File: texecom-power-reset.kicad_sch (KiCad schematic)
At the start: 0 parts

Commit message: Switch to on-board relays and add wired schematic
- Replace the off-board REL-2CHAN-335V relay module with two on-board
  SRD-05VDC-SL-C relays, 2N2222A drivers, 1N4007 flyback diodes and red
  indicator LEDs; remove J5-J7, the control lead and the Q/nQ links
- Redraw the schematic with wires (power symbols only for GND/+5V),
  ERC clean and netlist verified net by net
- Use a 74HCT4538 at 5V for the hardware timeout, with 1k GPIO series
  resistors and 100R CEXT power-down protection
- Update README (requirements, design, bench tests, decisions) and BOM
  (Micro Robotics / Communica sourcing with stock status)
- Keep earlier schematic versions in backup/ for reference
- Add .gitignore and .gitattributes (LF line endings for KiCad files)

Co-Authored-By: Claude Opus 5.5 <noreply@anthropic.com>
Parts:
- added C1: 100uF, Capacitor_THT:CP_Radial_D6.3mm_P2.50mm, symbol Device:C_Polarized
- added C2, C4, C7, C8: 100nF, Capacitor_THT:C_Disc_D5.0mm_W2.5mm_P5.00mm, symbol Device:C
- added C3: 10uF, Capacitor_THT:CP_Radial_D4.0mm_P1.50mm, symbol Device:C_Polarized
- added C5, C6: 10uF, Capacitor_SMD:C_1206_3216Metric_Pad1.33x1.80mm_HandSolder, symbol Device:C
- added D1, D3: 1N5822, Diode_THT:D_DO-201AD_P15.24mm_Horizontal, symbol Diode:1N5822
- added D2: P6KE18A, Diode_THT:D_DO-15_P10.16mm_Horizontal, symbol Device:D_Zener
- added D4, D5: 1N4007, Diode_THT:D_DO-41_SOD81_P10.16mm_Horizontal, symbol Device:D
- added D6, D7: RED, LED_THT:LED_D3.0mm, symbol Device:LED
- added F1: PTC 0.5A, Fuse:Fuse_1206_3216Metric_Pad1.42x1.75mm_HandSolder, symbol Device:Polyfuse
- added J1: BAT IN, TerminalBlock_Phoenix:TerminalBlock_Phoenix_MKDS-1,5-2_1x02_P5.00mm_Horizontal, symbol Connector:Screw_Terminal_01x02
- added J2: BAT OUT, TerminalBlock_Phoenix:TerminalBlock_Phoenix_MKDS-1,5-2_1x02_P5.00mm_Horizontal, symbol Connector:Screw_Terminal_01x02
- added J3: AC IN, TerminalBlock_Phoenix:TerminalBlock_Phoenix_MKDS-1,5-2_1x02_P5.00mm_Horizontal, symbol Connector:Screw_Terminal_01x02
- added J4: AC OUT, TerminalBlock_Phoenix:TerminalBlock_Phoenix_MKDS-1,5-2_1x02_P5.00mm_Horizontal, symbol Connector:Screw_Terminal_01x02
- added K1, K2: SRD-05VDC, Relay_THT:Relay_SPDT_SANYOU_SRD_Series_Form_C, symbol Relay:SANYOU_SRD_Form_C
- added MH1, MH2: M3, MountingHole:MountingHole_3.2mm_M3, symbol Mechanical:MountingHole
- added Q1, Q2: 2N2222A, Package_TO_SOT_THT:TO-92_Inline, symbol Transistor_BJT:PN2222A
- added R1, R2: 100k, Resistor_THT:R_Axial_DIN0207_L6.3mm_D2.5mm_P10.16mm_Horizontal, symbol Device:R
- added R10, R15, R16, R7, R8, R9: 1k, Resistor_SMD:R_1206_3216Metric_Pad1.30x1.75mm_HandSolder, symbol Device:R
- added R11, R12: 100, Resistor_SMD:R_1206_3216Metric_Pad1.30x1.75mm_HandSolder, symbol Device:R
- added R13, R14, R5, R6: 10k, Resistor_THT:R_Axial_DIN0207_L6.3mm_D2.5mm_P10.16mm_Horizontal, symbol Device:R
- added R3, R4: 1M, Resistor_THT:R_Axial_DIN0207_L6.3mm_D2.5mm_P10.16mm_Horizontal, symbol Device:R
- added U1: Pololu S9V11E2F5, texecom-power-reset:Pololu_S9V11E2x, symbol texecom-power-reset:Pololu_S9V11E2F5
- added U2: 74HCT4538, Package_DIP:DIP-16_W7.62mm_Socket, symbol 4xxx:4538
- added U3: ESP32-C3 SuperMini, texecom-power-reset:ESP32-C3-SuperMini, symbol texecom-power-reset:ESP32-C3-SuperMini
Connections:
- new net: F1.1, J1.1 (Pin_1), K1.1
- new net: D1.2 (A), F1.2
- new net: J3.1 (Pin_1), K2.1
- new net: D5.2 (A), D7.1 (K), K2.2, Q2.3 (C)
- new net: J4.1 (Pin_1), K2.4
- new net: C1.1, C2.1, D1.1 (K), D2.1 (K), U1.3 (VIN)
- new net: C8.1, R6.2, U2.12 (Clk+)
- new net: Q2.2 (B), R14.1, R8.2
- new net: C6.1, R4.2, U2.14 (RxCx)
- new net: C5.1, R3.2, U2.2 (RxCx)
- new net: R1.1, R5.1, R9.2, U2.3 (R)
- new net: C7.1, R5.2, U2.4 (Clk+)
- new net: R7.1, U2.6 (Q)
- new net: R10.1, U3.4 (IO4)
- new net: R9.1, U3.5 (IO3)
- new net: Q1.2 (B), R13.1, R7.2
- new net: D4.2 (A), D6.1 (K), K1.2, Q1.3 (C)
- new net: J3.2 (Pin_2), J4.2 (Pin_2)
- new net: R8.1, U2.10 (Q)
- new net: R10.2, R2.1, R6.1, U2.13 (R)
- new net: C6.2, R12.1
- new net: C5.2, R11.1
- new net: D7.2 (A), R16.2
- new net: D6.2 (A), R15.2
- new net: J2.1 (Pin_1), K1.4
- new net +5V: C3.1, C4.1, D3.2 (A), D4.1 (K), D5.1 (K), K1.5, K2.5, R15.1, R16.1, R3.1, R4.1, U1.1 (VOUT), U2.11 (Clk-), U2.16 (VDD), U2.5 (Clk-)
- new net +5V_MCU: D3.1 (K), U3.1 (5V)
- new net GND: C1.2, C2.2, C3.2, C4.2, C7.2, C8.2, D2.2 (A), J1.2 (Pin_2), J2.2 (Pin_2), Q1.1 (E), Q2.1 (E), R1.2, R11.2, R12.2, R13.2, R14.2, R2.2, U1.2 (GND), U2.1 (Cx), U2.15 (Cx), U2.8 (VSS), U3.2 (GND)
- no-connect marks 0 -> 17
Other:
- note added: "BAT_IN+ to relay K1 COM"
- note added: "CH1: battery relay K1 (GPIO3)"
- note added: "CH2: AC relay K2 (GPIO4)"
- note added: "CONTROLLER ESP32-C3 SuperMini (socketed)"
- note added: "HARDWARE TIMEOUT (74HCT4538 @ 5V) Relay ON = GPIO high AND < T since rising edge T = 0.7 x Rext x Cext = 0.7 x 1M x 10uF = ~7 s (Tasmota PulseTime 3.0 / 3.5 s is always shorter) R9/R10 1k: protect ESP GPIO if 5V rail is off (USB only) R11/R12 100R: TI rapid power-down protection for Cext RELAY DRIVERS Q -> R7/R8 1k -> 2N2222A (R13/R14 10k base pull-down) D4/D5 1N4007 flyback across each coil R15/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"
- note added: "PANEL AC (16VAC) J3 in -> K2 NC -> J4 out"
- note added: "PANEL BATTERY J1 in -> K1 NC -> J2 out"
- note added: "POWER: J1 battery tap (never switched) -> F1 PTC -> D1 reverse-polarity -> U1 Pololu 5V. D3 blocks USB backfeed from the SuperMini onto the +5V rail"
- note added: "U2C = power pins of U2 (same 74HCT4538 chip as U2A/U2B) Pin 16 VDD = +5V, pin 8 VSS = GND C4 100nF decoupling: place right beside pins 16 and 8 on the PCB"

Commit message: Add PCB rev A, milling footprints, fab files and project summary
- PCB rev A (92 x 70 mm, 2-layer, CNC-milled): placed and routed with the
  KiCad routing tools at 0.8 mm clearance, 15 wire-link vias, GND pours;
  DRC 0 violations / 0 unconnected, connectivity verified against schematic
- Milling footprint variants (oval enlarged pads; per-pad top keepouts on
  parts whose body covers the top pads) and custom .kicad_dru rules
- Schematic footprints assigned to the milling variants
- Gerbers (F.Cu, B.Cu, Edge.Cuts) and Excellon drill in fab/
- Copper renders and assembly drawing in docs/
- project-summary.html: one-page visual summary, linked from the README
- README: PCB section, drill table, assembly notes, decisions

Co-Authored-By: Claude Opus 5.5 <noreply@anthropic.com>
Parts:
- C1: footprint Capacitor_THT:CP_Radial_D6.3mm_P2.50mm -> texecom-power-reset:CP_Radial_D6.3mm_P2.50mm_Mill
- C2, C4, C7, C8: footprint Capacitor_THT:C_Disc_D5.0mm_W2.5mm_P5.00mm -> texecom-power-reset:C_Disc_D5.0mm_W2.5mm_P5.00mm_Mill
- C3: footprint Capacitor_THT:CP_Radial_D4.0mm_P1.50mm -> texecom-power-reset:CP_Radial_D5.0mm_P2.50mm_Mill
- D1, D3: footprint Diode_THT:D_DO-201AD_P15.24mm_Horizontal -> texecom-power-reset:D_DO-201AD_P15.24mm_Mill
- D2: footprint Diode_THT:D_DO-15_P10.16mm_Horizontal -> texecom-power-reset:D_DO-15_P10.16mm_Mill
- D4, D5: footprint Diode_THT:D_DO-41_SOD81_P10.16mm_Horizontal -> texecom-power-reset:D_DO-41_P10.16mm_Mill
- D6, D7: footprint LED_THT:LED_D3.0mm -> texecom-power-reset:LED_D3.0mm_Mill
- J1, J2, J3, J4: footprint TerminalBlock_Phoenix:TerminalBlock_Phoenix_MKDS-1,5-2_1x02_P5.00mm_Horizontal -> texecom-power-reset:KF301-2P_P5.00mm_Mill
- K1, K2: footprint Relay_THT:Relay_SPDT_SANYOU_SRD_Series_Form_C -> texecom-power-reset:Relay_SRD_Form_C_Mill
- Q1, Q2: footprint Package_TO_SOT_THT:TO-92_Inline -> texecom-power-reset:TO-92_Inline_Wide_Mill
- R1, R13, R14, R2, R3, R4, R5, R6: footprint Resistor_THT:R_Axial_DIN0207_L6.3mm_D2.5mm_P10.16mm_Horizontal -> texecom-power-reset:R_Axial_DIN0207_P10.16mm_Mill
- U1: footprint texecom-power-reset:Pololu_S9V11E2x -> texecom-power-reset:Pololu_S9V11E2x_Mill
- U2: footprint Package_DIP:DIP-16_W7.62mm_Socket -> texecom-power-reset:DIP-16_W7.62mm_Socket_Mill
- U3: footprint texecom-power-reset:ESP32-C3-SuperMini -> texecom-power-reset:ESP32-C3-SuperMini_Mill
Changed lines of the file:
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@@
 				)
     )
-    (property "Footprint" "TerminalBlock_Phoenix:TerminalBlock_Phoenix_MKDS-1,5-2_1x02_P5.00mm_Horizontal"
+    (property "Footprint" "texecom-power-reset:KF301-2P_P5.00mm_Mill"
       (at 20.32 50.8 0)
       (hide yes)
@@
 				)
     )
-    (property "Footprint" "Diode_THT:D_DO-201AD_P15.24mm_Horizontal"
+    (property "Footprint" "texecom-power-reset:D_DO-201AD_P15.24mm_Mill"
       (at 63.5 55.245 0)
       (hide yes)
@@
 					) (justify left))
     )
-    (property "Footprint" "Capacitor_THT:CP_Radial_D6.3mm_P2.50mm"
+    (property "Footprint" "texecom-power-reset:CP_Radial_D6.3mm_P2.50mm_Mill"
       (at 77.165 50.8 0)
       (hide yes)
@@
 					) (justify left))
     )
-    (property "Footprint" "Capacitor_THT:C_Disc_D5.0mm_W2.5mm_P5.00mm"
+    (property "Footprint" "texecom-power-reset:C_Disc_D5.0mm_W2.5mm_P5.00mm_Mill"
       (at 87.325 50.8 0)
       (hide yes)
@@
 					) (justify left))
     )
-    (property "Footprint" "Diode_THT:D_DO-15_P10.16mm_Horizontal"
+    (property "Footprint" "texecom-power-reset:D_DO-15_P10.16mm_Mill"
       (at 96.52 54.61 0)
       (hide yes)
@@
 				)
     )
-    (property "Footprint" "texecom-power-reset:Pololu_S9V11E2x"
+    (property "Footprint" "texecom-power-reset:Pololu_S9V11E2x_Mill"
       (at 121.92 48.26 0)
       (hide yes)
@@
 					) (justify left))
     )
-    (property "Footprint" "Capacitor_THT:CP_Radial_D4.0mm_P1.50mm"
+    (property "Footprint" "texecom-power-reset:CP_Radial_D5.0mm_P2.50mm_Mill"
       (at 140.665 50.8 0)
       (hide yes)
@@
 				)
     )
-    (property "Footprint" "Diode_THT:D_DO-201AD_P15.24mm_Horizontal"
+    (property "Footprint" "texecom-power-reset:D_DO-201AD_P15.24mm_Mill"
       (at 160.02 55.245 0)
       (hide yes)
@@
 				)
     )
-    (property "Footprint" "texecom-power-reset:ESP32-C3-SuperMini"
+    (property "Footprint" "texecom-power-reset:ESP32-C3-SuperMini_Mill"
       (at 48.26 190.5 0)
       (hide yes)
@@
 					) (justify left))
     )
-    (property "Footprint" "TerminalBlock_Phoenix:TerminalBlock_Phoenix_MKDS-1,5-2_1x02_P5.00mm_Horizontal"
+    (property "Footprint" "texecom-power-reset:KF301-2P_P5.00mm_Mill"
       (at 254 177.8 0)
       (hide yes)
@@
 					) (justify left))
     )
-    (property "Footprint" "TerminalBlock_Phoenix:TerminalBlock_Phoenix_MKDS-1,5-2_1x02_P5.00mm_Horizontal"
+    (property "Footprint" "texecom-power-reset:KF301-2P_P5.00mm_Mill"
       (at 254 91.44 0)
       (hide yes)
@@
 					) (justify left))
     )
-    (property "Footprint" "TerminalBlock_Phoenix:TerminalBlock_Phoenix_MKDS-1,5-2_1x02_P5.00mm_Horizontal"
+    (property "Footprint" "texecom-power-reset:KF301-2P_P5.00mm_Mill"
       (at 254 71.12 0)
       (hide yes)
@@
 					) (justify left))
     )
-    (property "Footprint" "Capacitor_THT:C_Disc_D5.0mm_W2.5mm_P5.00mm"
+    (property "Footprint" "texecom-power-reset:C_Disc_D5.0mm_W2.5mm_P5.00mm_Mill"
       (at 336.245 120.65 0)
       (hide yes)
@@
 					) (justify left))
     )
-    (property "Footprint" "Resistor_THT:R_Axial_DIN0207_L6.3mm_D2.5mm_P10.16mm_Horizontal"
+    (property "Footprint" "texecom-power-reset:R_Axial_DIN0207_P10.16mm_Mill"
       (at 97.282 118.11 90)
       (hide yes)
@@
 				)
     )
-    (property "Footprint" "Resistor_THT:R_Axial_DIN0207_L6.3mm_D2.5mm_P10.16mm_Horizontal"
+    (property "Footprint" "texecom-power-reset:R_Axial_DIN0207_P10.16mm_Mill"
       (at 107.95 103.378 90)
       (hide yes)
@@
 					) (justify left))
     )
-    (property "Footprint" "Capacitor_THT:C_Disc_D5.0mm_W2.5mm_P5.00mm"
+    (property "Footprint" "texecom-power-reset:C_Disc_D5.0mm_W2.5mm_P5.00mm_Mill"
       (at 125.425 101.6 0)
       (hide yes)
@@
 					) (justify right))
     )
-    (property "Footprint" "Resistor_THT:R_Axial_DIN0207_L6.3mm_D2.5mm_P10.16mm_Horizontal"
+    (property "Footprint" "texecom-power-reset:R_Axial_DIN0207_P10.16mm_Mill"
       (at 178.562 82.55 90)
       (hide yes)
@@
 					) (justify left))
     )
-    (property "Footprint" "Resistor_THT:R_Axial_DIN0207_L6.3mm_D2.5mm_P10.16mm_Horizontal"
+    (property "Footprint" "texecom-power-reset:R_Axial_DIN0207_P10.16mm_Mill"
       (at 201.422 107.95 90)
       (hide yes)
@@
     				) (justify left))
     )
-    (property "Footprint" "Package_TO_SOT_THT:TO-92_Inline"
+    (property "Footprint" "texecom-power-reset:TO-92_Inline_Wide_Mill"
       (at 215.9 102.235 0)
       (hide yes)
@@
     				) (justify left))
     )
-    (property "Footprint" "Relay_THT:Relay_SPDT_SANYOU_SRD_Series_Form_C"
+    (property "Footprint" "texecom-power-reset:Relay_SRD_Form_C_Mill"
       (at 229.87 82.55 0)
       (hide yes)
@@
     				) (justify right))
     )
-    (property "Footprint" "Diode_THT:D_DO-41_SOD81_P10.16mm_Horizontal"
+    (property "Footprint" "texecom-power-reset:D_DO-41_P10.16mm_Mill"
       (at 205.74 83.82 0)
       (hide yes)
@@
     				) (justify right))
     )
-    (property "Footprint" "LED_THT:LED_D3.0mm"
+    (property "Footprint" "texecom-power-reset:LED_D3.0mm_Mill"
       (at 198.12 87.63 0)
       (hide yes)
@@
 					) (justify left))
     )
-    (property "Footprint" "Resistor_THT:R_Axial_DIN0207_L6.3mm_D2.5mm_P10.16mm_Horizontal"
+    (property "Footprint" "texecom-power-reset:R_Axial_DIN0207_P10.16mm_Mill"
       (at 97.282 224.79 90)
       (hide yes)
@@
 				)
     )
-    (property "Footprint" "Resistor_THT:R_Axial_DIN0207_L6.3mm_D2.5mm_P10.16mm_Horizontal"
+    (property "Footprint" "texecom-power-reset:R_Axial_DIN0207_P10.16mm_Mill"
       (at 107.95 210.058 90)
       (hide yes)
@@
 					) (justify left))
     )
-    (property "Footprint" "Capacitor_THT:C_Disc_D5.0mm_W2.5mm_P5.00mm"
+    (property "Footprint" "texecom-power-reset:C_Disc_D5.0mm_W2.5mm_P5.00mm_Mill"
       (at 125.425 208.28 0)
       (hide yes)
@@
 					) (justify right))
     )
-    (property "Footprint" "Resistor_THT:R_Axial_DIN0207_L6.3mm_D2.5mm_P10.16mm_Horizontal"
+    (property "Footprint" "texecom-power-reset:R_Axial_DIN0207_P10.16mm_Mill"
       (at 178.562 189.23 90)
       (hide yes)
@@
 					) (justify left))
     )
-    (property "Footprint" "Resistor_THT:R_Axial_DIN0207_L6.3mm_D2.5mm_P10.16mm_Horizontal"
+    (property "Footprint" "texecom-power-reset:R_Axial_DIN0207_P10.16mm_Mill"
       (at 201.422 214.63 90)
       (hide yes)
@@
     				) (justify left))
     )
-    (property "Footprint" "Package_TO_SOT_THT:TO-92_Inline"
+    (property "Footprint" "texecom-power-reset:TO-92_Inline_Wide_Mill"
       (at 215.9 208.915 0)
       (hide yes)
@@
     				) (justify left))
     )
-    (property "Footprint" "Relay_THT:Relay_SPDT_SANYOU_SRD_Series_Form_C"
+    (property "Footprint" "texecom-power-reset:Relay_SRD_Form_C_Mill"
       (at 229.87 189.23 0)
       (hide yes)
@@
     				) (justify right))
     )
-    (property "Footprint" "Diode_THT:D_DO-41_SOD81_P10.16mm_Horizontal"
+    (property "Footprint" "texecom-power-reset:D_DO-41_P10.16mm_Mill"
       (at 205.74 190.5 0)
       (hide yes)
@@
     				) (justify right))
     )
-    (property "Footprint" "LED_THT:LED_D3.0mm"
+    (property "Footprint" "texecom-power-reset:LED_D3.0mm_Mill"
       (at 198.12 194.31 0)
       (hide yes)
@@
 				)
     )
-    (property "Footprint" "Package_DIP:DIP-16_W7.62mm_Socket"
+    (property "Footprint" "texecom-power-reset:DIP-16_W7.62mm_Socket_Mill"
       (at 175.26 214.63 0)
       (hide yes)
@@
 				)
     )
-    (property "Footprint" "Package_DIP:DIP-16_W7.62mm_Socket"
+    (property "Footprint" "texecom-power-reset:DIP-16_W7.62mm_Socket_Mill"
       (at 175.26 107.95 0)
       (hide yes)
@@
 					) (justify right))
     )
-    (property "Footprint" "Package_DIP:DIP-16_W7.62mm_Socket"
+    (property "Footprint" "texecom-power-reset:DIP-16_W7.62mm_Socket_Mill"
       (at 325.12 125.73 0)
       (hide yes)

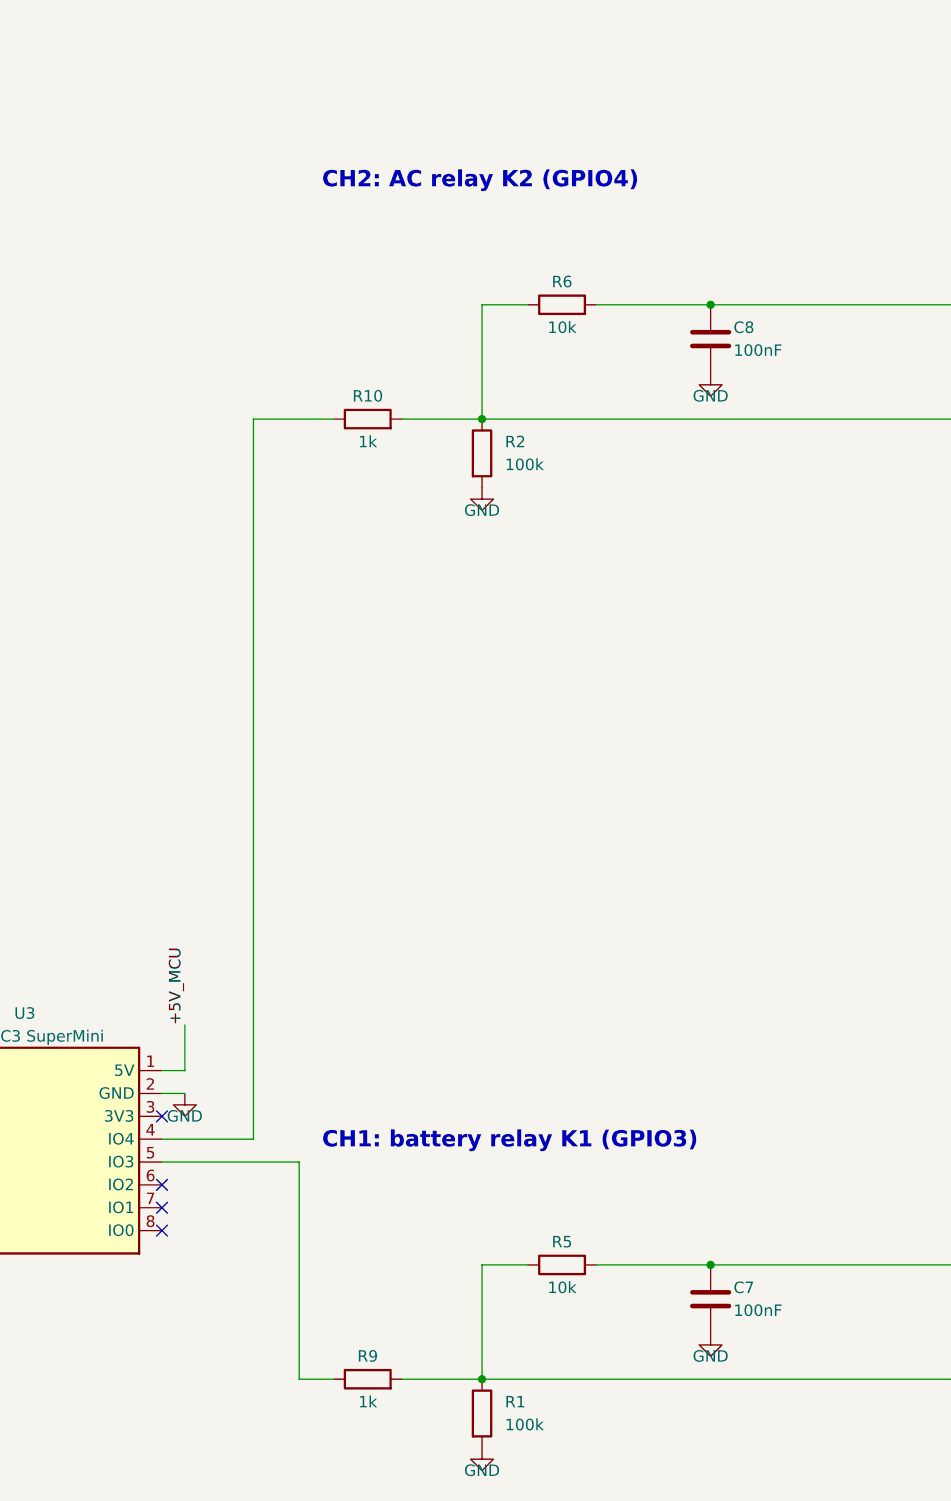
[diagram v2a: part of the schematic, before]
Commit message: Correct mirrored SuperMini footprint; rotate U3, swap GPIO3/GPIO4
- ESP32-C3-SuperMini footprints: pin rows were mirrored (matched the
  bottom-view pinout drawing); corrected so the module mounts button
  side up
- U3 rotated 180 deg: USB-C at the board edge, original routing kept
  (DRC 0/0, 16 vias); antenna keepout removed
- Schematic: GPIO4 -> channel 1 (K1 battery), GPIO3 -> channel 2 (K2 AC)
- Legend: "USB ->" arrow on U3
- BOM: optional Communica IPEX WiFi antenna
- README (Tasmota GPIO table, V2 WS2812 on GPIO8, orientation,
  decisions), regenerated fab/, docs/, schematic PDF and summary

Co-Authored-By: Claude Opus 5.5 <noreply@anthropic.com>
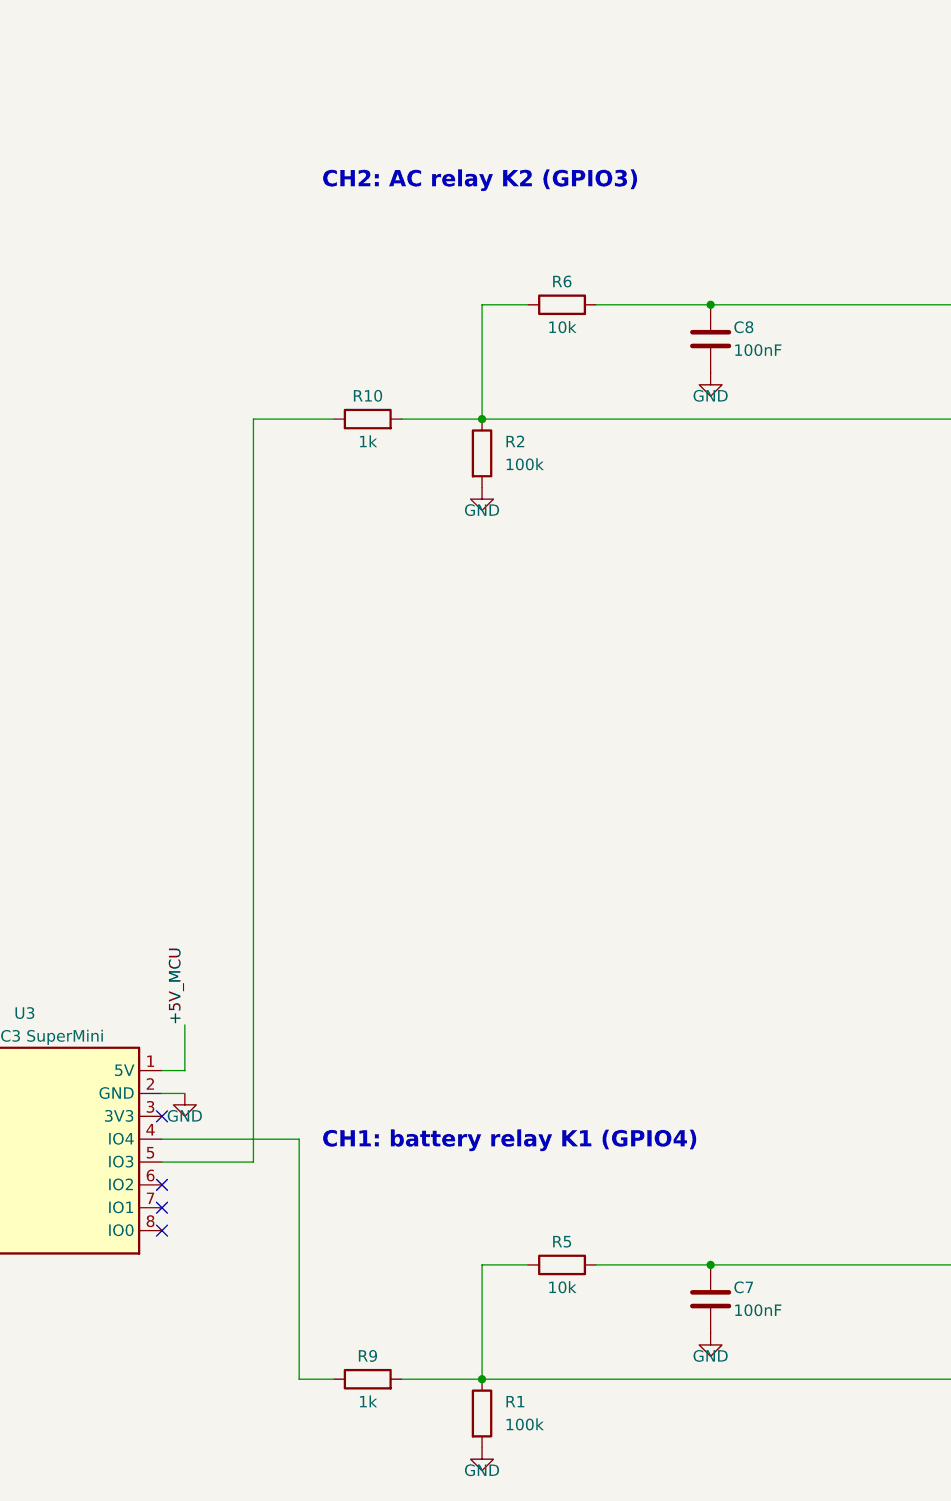
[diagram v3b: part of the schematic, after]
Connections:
- net at U3.4 (IO4): now also R9.1; no longer R10.1
- net at U3.5 (IO3): now also R10.1; no longer R9.1
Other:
- note added: "CH1: battery relay K1 (GPIO4)"
- note added: "CH2: AC relay K2 (GPIO3)"
- note removed: "CH1: battery relay K1 (GPIO3)"
- note removed: "CH2: AC relay K2 (GPIO4)"
